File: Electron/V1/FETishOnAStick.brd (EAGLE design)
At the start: 89.5 x 29.3 mm, 18 parts, among them Q1 FDD8780 or FDD8451, Q2 BSS138 - 200mA/50V, Q3 FDD8780 or FDD8451

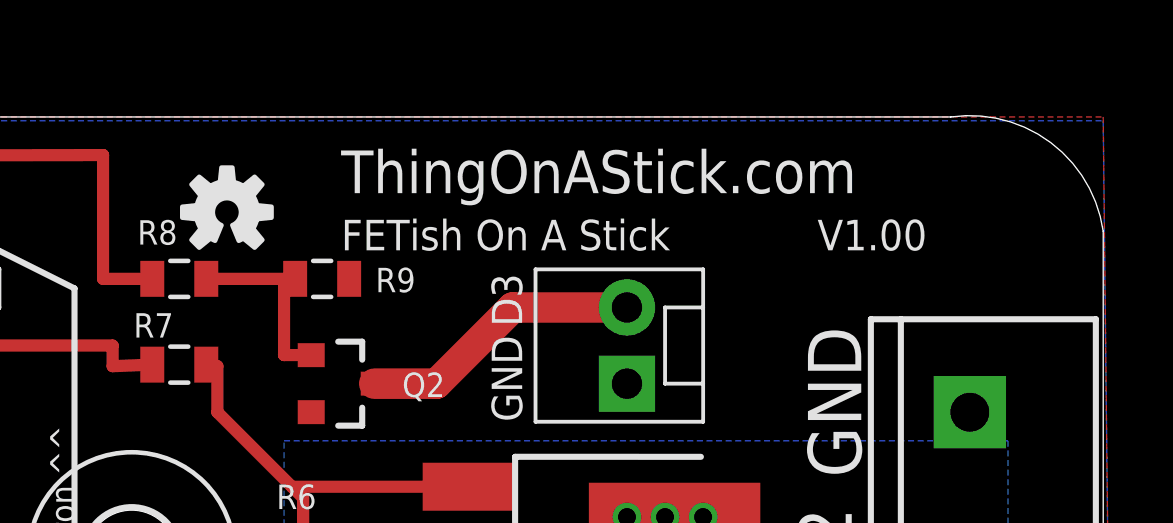
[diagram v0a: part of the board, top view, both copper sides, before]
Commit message: Moved OSH logo
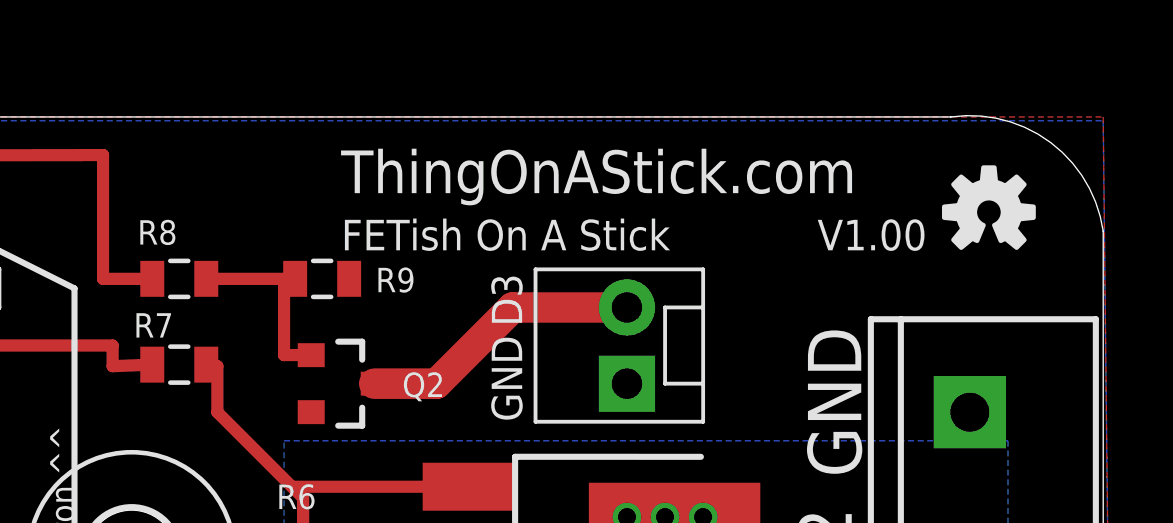
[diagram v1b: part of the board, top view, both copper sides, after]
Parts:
- moved LOGO2 25.4 mm to (101.0, 24.1)
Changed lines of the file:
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@@
 <grid distance="0.05" unitdist="inch" unit="inch" style="lines" multiple="1" display="yes" altdistance="0.0125" altunitdist="inch" altunit="inch"/>
 <layers>
-<layer number="1" name="Top" color="4" fill="1" visible="no" active="yes"/>
+<layer number="1" name="Top" color="4" fill="1" visible="yes" active="yes"/>
 <layer number="2" name="Route2" color="1" fill="3" visible="no" active="no"/>
 <layer number="3" name="Route3" color="4" fill="3" visible="no" active="no"/>
@@
 <elements>
 <element name="CONN1" library="SparkFun-Connectors" package="USB-A-SMT-MALE" value="USBA-SMD-MALE" x="14.605" y="12.7" smashed="yes" rot="R90"/>
-<element name="LOGO2" library="SparkFun-Aesthetics" package="OSHW-LOGO-S" value="OSHW-LOGOS" x="75.565" y="24.13"/>
+<element name="LOGO2" library="SparkFun-Aesthetics" package="OSHW-LOGO-S" value="OSHW-LOGOS" x="100.965" y="24.13"/>
 <element name="JP1" library="SparkFun-Connectors" package="SCREWTERMINAL-5MM-3" value="" x="100.33" y="17.4625" locked="yes" smashed="yes" rot="R270">
 <attribute name="STOREFRONT_ID" value="PRT-08433" x="100.33" y="17.4625" size="1.778" layer="27" rot="R270" display="off"/>
